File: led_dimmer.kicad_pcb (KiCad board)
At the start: 2 copper layers, 23.5 x 25.1 mm, 13 parts, among them P1 CONN_2, P2 CONN_2, Q1 MOSFET_N, U1 555

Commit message: tweaks
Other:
- net class Default: clearance 0.3048 -> 0.254; trace_width 0.3048 -> 0.254; via_dia 0.8 -> 0.86; via_drill 0.3 -> 0.4
- rule trace_clearance: 0.3048 -> 0.254
- rule trace_min: 0.3048 -> 0.254
- rule via_min_drill: 0.3 -> 0.4
- rule via_min_size: 0.8 -> 0.86
- board text added: "PWR 12V"
- board text removed: "PWR"
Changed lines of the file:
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@@
-(kicad_pcb (version 3) (host pcbnew "(2014-01-30 BZR 4648)-product")
+(kicad_pcb (version 3) (host pcbnew "(2014-01-10 BZR 4619)-product")
   (general
     (links 24)
@@
   )
   (setup
-    (last_trace_width 0.3048)
+    (last_trace_width 0.254)
     (user_trace_width 0.6096)
     (user_trace_width 1.6256)
-    (trace_clearance 0.3048)
+    (trace_clearance 0.254)
     (zone_clearance 0.2794)
     (zone_45_only no)
-    (trace_min 0.3048)
+    (trace_min 0.254)
     (segment_width 0.2)
     (edge_width 0.1)
-    (via_size 0.8)
-    (via_drill 0.3)
-    (via_min_size 0.8)
-    (via_min_drill 0.3)
+    (via_size 0.86)
+    (via_drill 0.4)
+    (via_min_size 0.86)
+    (via_min_drill 0.4)
     (uvia_size 0.508)
     (uvia_drill 0.127)
@@
     (pcbplotparams
       (layerselection 3178497)
-      (usegerberextensions true)
+      (usegerberextensions false)
       (excludeedgelayer true)
       (linewidth 0.150000)
@@
       (psa4output false)
       (plotreference true)
-      (plotvalue true)
+      (plotvalue false)
       (plotothertext true)
       (plotinvisibletext false)
       (padsonsilk false)
       (subtractmaskfromsilk false)
-      (outputformat 1)
+      (outputformat 2)
       (mirror false)
       (drillshape 0)
       (scaleselection 1)
-      (outputdirectory ""))
+      (outputdirectory /tmp))
   )
   (net 0 "")
@@
   (net 10 VCC)
   (net_class Default "This is the default net class."
-    (clearance 0.3048)
-    (trace_width 0.3048)
-    (via_dia 0.8)
-    (via_drill 0.3)
+    (clearance 0.254)
+    (trace_width 0.254)
+    (via_dia 0.86)
+    (via_drill 0.4)
     (uvia_dia 0.508)
     (uvia_drill 0.127)
@@
     (at 164.465 102.87 270)
     (descr "grid 3.5mm, diameter 8mm")
-    (fp_text reference C1 (at 3.175 -3.81 270) (layer F.SilkS)
+    (fp_text reference C1 (at 0 2.54 270) (layer F.SilkS)
       (effects (font (size 1 1) (thickness 0.18)))
     )
@@
   (module ds:minimelf (layer F.Cu)
     (at 165.4175 110.8075 90)
-    (fp_text reference D1 (at 3.81 0 180) (layer F.SilkS)
+    (fp_text reference D1 (at 0 3.175 180) (layer F.SilkS)
       (effects (font (size 1 1) (thickness 0.18)))
     )
@@
     )
   )
-  (gr_text PWR (at 172.72 107.315) (layer B.SilkS)
+  (gr_text "PWR\n12V" (at 169.2275 107.95) (layer B.SilkS)
     (effects (font (size 1.5 1.5) (thickness 0.3)) (justify mirror))
   )
-  (gr_text LED (at 156.21 107.315) (layer B.SilkS)
+  (gr_text LED (at 159.385 106.68) (layer B.SilkS)
     (effects (font (size 1.5 1.5) (thickness 0.3)) (justify mirror))
   )
-  (gr_text "LED\ndimmer" (at 163.83 116.205 90) (layer B.SilkS)
+  (gr_text "LED\ndimmer" (at 161.925 116.205 90) (layer B.SilkS)
     (effects (font (size 2 2) (thickness 0.3)) (justify mirror))
   )
@@
   (segment (start 155.6 114.3) (end 155.575 114.275) (width 0.3048) (layer F.Cu) (net 1) (status 30))
   (segment (start 155.575 114.275) (end 155.575 113.3475) (width 0.3048) (layer F.Cu) (net 1) (status 10))
-  (via (at 155.575 113.3475) (size 0.8) (layers F.Cu B.Cu) (net 1))
+  (via (at 155.575 113.3475) (size 0.86) (layers F.Cu B.Cu) (net 1))
   (segment (start 159.512 119.5705) (end 159.7025 119.38) (width 0.3048) (layer F.Cu) (net 1))
   (segment (start 159.512 120.65) (end 159.512 119.5705) (width 0.3048) (layer F.Cu) (net 1) (status 10))
-  (via (at 159.7025 119.38) (size 0.8) (layers F.Cu B.Cu) (net 1))
+  (via (at 159.7025 119.38) (size 0.86) (layers F.Cu B.Cu) (net 1))
   (segment (start 157.285 107.635) (end 157.285 106.875) (width 1.6256) (layer F.Cu) (net 1) (status 10))
   (segment (start 157.285 106.875) (end 159.54 104.62) (width 1.6256) (layer F.Cu) (net 1))
@@
   (segment (start 157.6425 104.62) (end 156.21 104.62) (width 0.6096) (layer B.Cu) (net 4) (status 20))
   (segment (start 160.02 106.9975) (end 157.6425 104.62) (width 0.6096) (layer B.Cu) (net 4))
-  (via (at 160.02 106.9975) (size 0.8) (layers F.Cu B.Cu) (net 4))
+  (via (at 160.02 106.9975) (size 0.86) (layers F.Cu B.Cu) (net 4))
   (segment (start 160.147 107.1245) (end 160.02 106.9975) (width 0.6096) (layer F.Cu) (net 4))
   (segment (start 155.135 108.585) (end 155.135 105.695) (width 1.6256) (layer F.Cu) (net 4) (status 10))
   (segment (start 155.135 105.695) (end 156.21 104.62) (width 1.6256) (layer F.Cu) (net 4) (status 20))
-  (segment (start 158.115 113.3475) (end 159.7025 111.76) (width 0.3048) (layer F.Cu) (net 5) (status 20))
-  (segment (start 159.0675 115.57) (end 158.115 114.6175) (width 0.3048) (layer F.Cu) (net 5))
-  (segment (start 158.115 114.6175) (end 158.115 113.3475) (width 0.3048) (layer F.Cu) (net 5))
-  (segment (start 160.63 115.57) (end 159.0675 115.57) (width 0.3048) (layer F.Cu) (net 5) (status 10))
+  (segment (start 157.7975 113.665) (end 159.7025 111.76) (width 0.3048) (layer F.Cu) (net 5) (status 20))
+  (segment (start 158.75 115.57) (end 157.7975 114.6175) (width 0.3048) (layer F.Cu) (net 5))
+  (segment (start 157.7975 114.6175) (end 157.7975 113.665) (width 0.3048) (layer F.Cu) (net 5))
+  (segment (start 160.63 115.57) (end 158.75 115.57) (width 0.3048) (layer F.Cu) (net 5) (status 10))
   (segment (start 159.7025 111.76) (end 160.147 111.76) (width 0.3048) (layer F.Cu) (net 5) (status 30))
   (segment (start 165.4175 112.7825) (end 165.4175 116.135) (width 0.3048) (layer F.Cu) (net 5) (status 30))
@@
   (segment (start 153.9875 112.8395) (end 153.9875 116.5225) (width 0.3048) (layer F.Cu) (net 9))
   (segment (start 153.9875 116.5225) (end 154.305 116.84) (width 0.3048) (layer F.Cu) (net 9))
+  (segment (start 160.63 114.3) (end 158.75 114.3) (width 0.3048) (layer F.Cu) (net 10))
+  (segment (start 157.7975 115.2525) (end 157.7975 117.1575) (width 0.3048) (layer B.Cu) (net 10))
+  (via (at 157.7975 117.1575) (size 0.86) (layers F.Cu B.Cu) (net 10))
+  (segment (start 157.7975 117.1575) (end 156.845 118.11) (width 0.3048) (layer F.Cu) (net 10))
+  (segment (start 156.845 118.11) (end 155.6 118.11) (width 0.3048) (layer F.Cu) (net 10) (status 20))
+  (segment (start 158.75 114.3) (end 157.7975 115.2525) (width 0.3048) (layer B.Cu) (net 10))
+  (via (at 158.75 114.3) (size 0.86) (layers F.Cu B.Cu) (net 10))
   (segment (start 162.433 111.76) (end 162.433 111.5695) (width 0.3048) (layer F.Cu) (net 10) (status 30))
   (segment (start 166.6875 103.3425) (end 164.465 101.12) (width 0.3048) (layer B.Cu) (net 10) (status 20))
   (segment (start 166.6875 107.315) (end 166.6875 103.3425) (width 0.3048) (layer B.Cu) (net 10))
   (segment (start 163.5125 110.49) (end 166.6875 107.315) (width 0.3048) (layer B.Cu) (net 10))
-  (via (at 163.5125 110.49) (size 0.8) (layers F.Cu B.Cu) (net 10))
+  (via (at 163.5125 110.49) (size 0.86) (layers F.Cu B.Cu) (net 10))
   (segment (start 162.433 111.5695) (end 163.5125 110.49) (width 0.3048) (layer F.Cu) (net 10) (status 10))
   (segment (start 162.433 111.76) (end 162.433 112.497) (width 0.3048) (layer F.Cu) (net 10) (status 10))
   (segment (start 162.433 112.497) (end 160.63 114.3) (width 0.3048) (layer F.Cu) (net 10) (status 20))
-  (segment (start 160.63 114.3) (end 159.0675 114.3) (width 0.3048) (layer F.Cu) (net 10) (status 10))
-  (segment (start 156.845 118.11) (end 155.6 118.11) (width 0.3048) (layer F.Cu) (net 10) (status 20))
-  (segment (start 157.48 117.475) (end 156.845 118.11) (width 0.3048) (layer F.Cu) (net 10))
-  (via (at 157.48 117.475) (size 0.8) (layers F.Cu B.Cu) (net 10))
-  (segment (start 157.48 115.8875) (end 157.48 117.475) (width 0.3048) (layer B.Cu) (net 10))
-  (segment (start 159.0675 114.3) (end 157.48 115.8875) (width 0.3048) (layer B.Cu) (net 10))
-  (via (at 159.0675 114.3) (size 0.8) (layers F.Cu B.Cu) (net 10))
   (segment (start 162.433 108.585) (end 162.56 108.458) (width 0.6096) (layer F.Cu) (net 10) (status 30))
   (segment (start 162.56 108.458) (end 162.56 106.68) (width 0.6096) (layer F.Cu) (net 10) (status 10))
   (segment (start 157 101.12) (end 156.21 101.12) (width 0.6096) (layer B.Cu) (net 10) (status 30))
   (segment (start 162.56 106.68) (end 157 101.12) (width 0.6096) (layer B.Cu) (net 10) (status 20))
-  (via (at 162.56 106.68) (size 0.8) (layers F.Cu B.Cu) (net 10))
+  (via (at 162.56 106.68) (size 0.86) (layers F.Cu B.Cu) (net 10))
   (segment (start 156.21 101.12) (end 164.465 101.12) (width 1.6256) (layer F.Cu) (net 10) (status 30))
   (segment (start 164.465 101.12) (end 172.72 101.12) (width 1.6256) (layer F.Cu) (net 10) (status 30))

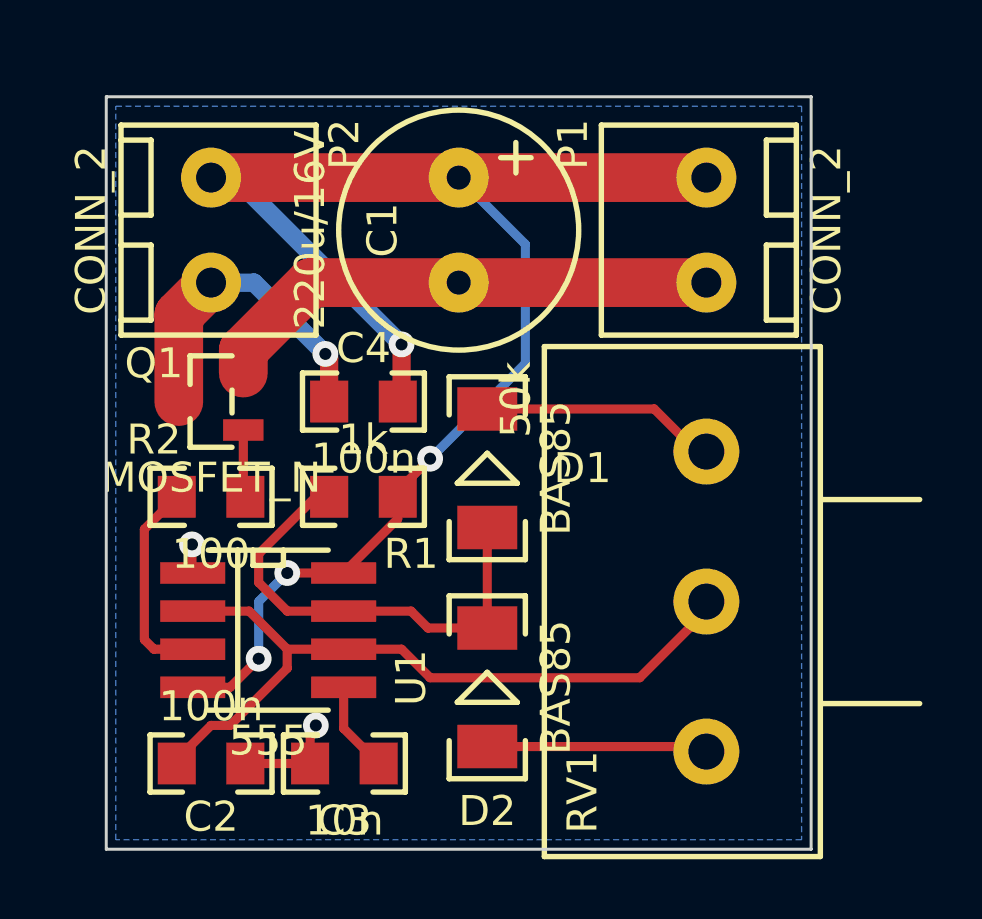
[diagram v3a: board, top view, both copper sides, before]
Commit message: bottom silk fixes, power connector turned
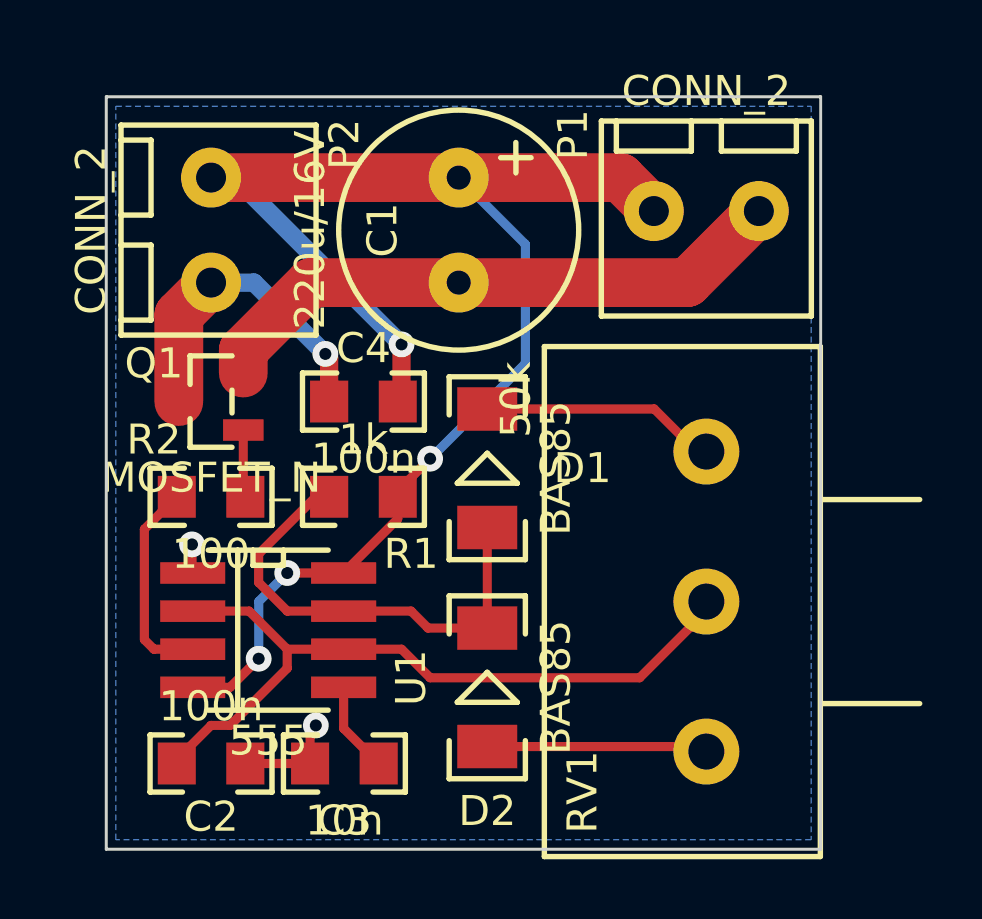
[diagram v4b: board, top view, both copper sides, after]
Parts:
- moved P1 0.64 mm to (172.7, 102.2), turned to 180 degrees
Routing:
- net GND: track 21.8 -> 24.5 mm
- net VCC: track 51.5 -> 50.2 mm
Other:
- board size 23.5 x 25.1 mm -> 23.8 x 25.1 mm
- board text added: "https://github.com/ dsiroky/led_dimmer"
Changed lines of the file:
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@@
-(kicad_pcb (version 3) (host pcbnew "(2014-01-10 BZR 4619)-product")
+(kicad_pcb (version 3) (host pcbnew "(2014-01-30 BZR 4648)-product")
   (general
     (links 24)
     (no_connects 0)
-    (area 148.886629 97.965 180.226801 124.147301)
+    (area 148.937429 97.011 180.176001 124.096501)
     (thickness 1.6)
-    (drawings 11)
-    (tracks 74)
+    (drawings 12)
+    (tracks 76)
     (zones 0)
     (modules 13)
@@
   )
   (module ds:ark550_2ex (layer F.Cu)
-    (at 172.72 102.87 90)
-    (fp_text reference P1 (at 2.8575 -4.445 90) (layer F.SilkS)
-      (effects (font (size 1 1) (thickness 0.18)))
-    )
-    (fp_text value CONN_2 (at 0 4 90) (layer F.SilkS)
+    (at 172.72 102.235 180)
+    (fp_text reference P1 (at 4.445 2.54 270) (layer F.SilkS)
+      (effects (font (size 1 1) (thickness 0.18)))
+    )
+    (fp_text value CONN_2 (at 0 4 180) (layer F.SilkS)
       (effects (font (size 1 1) (thickness 0.18)))
     )
@@
     (fp_line (start 3.5 3) (end -3.5 3) (layer F.SilkS) (width 0.18))
     (fp_line (start -3.5 -3.5) (end -3.5 3) (layer F.SilkS) (width 0.18))
-    (pad 1 thru_hole circle (at -1.75 0 90) (size 2 2) (drill 1) (layers *.Cu *.Mask F.SilkS)
+    (pad 1 thru_hole circle (at -1.75 0 180) (size 2 2) (drill 1) (layers *.Cu *.Mask F.SilkS)
       (net 1 GND))
-    (pad 2 thru_hole circle (at 1.75 0 90) (size 2 2) (drill 1) (layers *.Cu *.Mask F.SilkS)
+    (pad 2 thru_hole circle (at 1.75 0 180) (size 2 2) (drill 1) (layers *.Cu *.Mask F.SilkS)
       (net 10 VCC))
   )
@@
     )
   )
-  (gr_text "PWR\n12V" (at 169.2275 107.95) (layer B.SilkS)
+  (gr_text "https://github.com/\n  dsiroky/led_dimmer" (at 161.925 121.6025) (layer B.SilkS)
+    (effects (font (size 1 1) (thickness 0.15)) (justify mirror))
+  )
+  (gr_text "PWR\n12V" (at 169.545 106.3625) (layer B.SilkS)
     (effects (font (size 1.5 1.5) (thickness 0.3)) (justify mirror))
   )
@@
     (effects (font (size 1.5 1.5) (thickness 0.3)) (justify mirror))
   )
-  (gr_text "LED\ndimmer" (at 161.925 116.205 90) (layer B.SilkS)
-    (effects (font (size 2 2) (thickness 0.3)) (justify mirror))
-  )
-  (gr_text - (at 169.545 104.4575) (layer B.SilkS)
+  (gr_text "LED\ndimmer" (at 165.1 115.2525) (layer B.SilkS)
+    (effects (font (size 1.8 1.8) (thickness 0.3)) (justify mirror))
+  )
+  (gr_text - (at 174.3075 99.695) (layer B.SilkS)
     (effects (font (size 3 3) (thickness 0.6)) (justify mirror))
   )
@@
     (effects (font (size 3 3) (thickness 0.6)) (justify mirror))
   )
-  (gr_text + (at 169.545 100.965) (layer B.SilkS)
+  (gr_text + (at 168.91 100.0125) (layer B.SilkS)
     (effects (font (size 3 3) (thickness 0.6)) (justify mirror))
   )
@@
     (effects (font (size 3 3) (thickness 0.6)) (justify mirror))
   )
-  (gr_line (start 176.2125 123.5075) (end 176.2125 98.425) (angle 90) (layer Edge.Cuts) (width 0.1))
+  (gr_line (start 176.53 123.5075) (end 176.53 98.425) (angle 90) (layer Edge.Cuts) (width 0.1))
   (gr_line (start 152.7175 98.425) (end 152.7175 123.5075) (angle 90) (layer Edge.Cuts) (width 0.1))
-  (gr_line (start 176.2125 98.425) (end 152.7175 98.425) (angle 90) (layer Edge.Cuts) (width 0.1))
-  (gr_line (start 152.7175 123.5075) (end 176.2125 123.5075) (angle 90) (layer Edge.Cuts) (width 0.1))
+  (gr_line (start 176.53 98.425) (end 152.7175 98.425) (angle 90) (layer Edge.Cuts) (width 0.1))
+  (gr_line (start 152.7175 123.5075) (end 176.53 123.5075) (angle 90) (layer Edge.Cuts) (width 0.1))
+  (segment (start 164.465 104.62) (end 172.085 104.62) (width 1.6256) (layer F.Cu) (net 1))
+  (segment (start 172.085 104.62) (end 174.47 102.235) (width 1.6256) (layer F.Cu) (net 1))
+  (segment (start 157.285 107.635) (end 157.285 106.875) (width 1.6256) (layer F.Cu) (net 1) (status 10))
+  (segment (start 157.285 106.875) (end 159.54 104.62) (width 1.6256) (layer F.Cu) (net 1))
+  (segment (start 159.54 104.62) (end 164.465 104.62) (width 1.6256) (layer F.Cu) (net 1) (status 20))
   (segment (start 164.465 104.62) (end 164.465 104.775) (width 0.3048) (layer B.Cu) (net 1) (status 30))
   (segment (start 155.6 114.3) (end 155.575 114.275) (width 0.3048) (layer F.Cu) (net 1) (status 30))
@@
   (segment (start 159.512 120.65) (end 159.512 119.5705) (width 0.3048) (layer F.Cu) (net 1) (status 10))
   (via (at 159.7025 119.38) (size 0.86) (layers F.Cu B.Cu) (net 1))
-  (segment (start 157.285 107.635) (end 157.285 106.875) (width 1.6256) (layer F.Cu) (net 1) (status 10))
-  (segment (start 157.285 106.875) (end 159.54 104.62) (width 1.6256) (layer F.Cu) (net 1))
-  (segment (start 159.54 104.62) (end 164.465 104.62) (width 1.6256) (layer F.Cu) (net 1) (status 20))
-  (segment (start 164.465 104.62) (end 172.72 104.62) (width 1.6256) (layer F.Cu) (net 1) (status 30))
   (segment (start 157.353 120.65) (end 159.512 120.65) (width 0.3048) (layer F.Cu) (net 1) (status 30))
   (segment (start 158.75 116.84) (end 158.75 117.475) (width 0.3048) (layer F.Cu) (net 2))
@@
   (segment (start 153.9875 112.8395) (end 153.9875 116.5225) (width 0.3048) (layer F.Cu) (net 9))
   (segment (start 153.9875 116.5225) (end 154.305 116.84) (width 0.3048) (layer F.Cu) (net 9))
+  (segment (start 164.465 101.12) (end 169.855 101.12) (width 1.6256) (layer F.Cu) (net 10))
+  (segment (start 169.855 101.12) (end 170.97 102.235) (width 1.6256) (layer F.Cu) (net 10))
   (segment (start 160.63 114.3) (end 158.75 114.3) (width 0.3048) (layer F.Cu) (net 10))
   (segment (start 157.7975 115.2525) (end 157.7975 117.1575) (width 0.3048) (layer B.Cu) (net 10))
@@
   (via (at 162.56 106.68) (size 0.86) (layers F.Cu B.Cu) (net 10))
   (segment (start 156.21 101.12) (end 164.465 101.12) (width 1.6256) (layer F.Cu) (net 10) (status 30))
-  (segment (start 164.465 101.12) (end 172.72 101.12) (width 1.6256) (layer F.Cu) (net 10) (status 30))
   (zone (net 1) (net_name GND) (layer B.Cu) (hatch edge 0.508)
     (connect_pads (clearance 0.2794))
@@
     (polygon
       (pts
-        (xy 175.895 123.19) (xy 153.035 123.19) (xy 153.035 98.7425) (xy 175.895 98.7425)
+        (xy 176.2125 123.19) (xy 153.035 123.19) (xy 153.035 98.7425) (xy 176.2125 98.7425)
       )
     )
